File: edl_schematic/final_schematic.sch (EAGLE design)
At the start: 296 parts, among them IC1 FT232RL, IC14 TL084D, IC15 TL084D, IC16 TL084D, IC17 TL084D, IC18 TL084D, IC19 TL084D, IC20 TL084D, IC21 TL084D, IC22 TL084D, IC23 TL084D, IC24 TL084D, IC25 TL084D, IC26 TL084D, IC27 TL084D, IC28 TL084D, IC29 TL084D, IC3 TL084D, IC30 TL084D, IC4 TPS77333, IC5 TL084D, IC6 7812TV, Q1 BC558B, U1 TMS320F28069_PN_80, U3 TLV5610_DW_20, U4 MAX395EWG, U6 MAX395EWG, U7 MAX395EWG

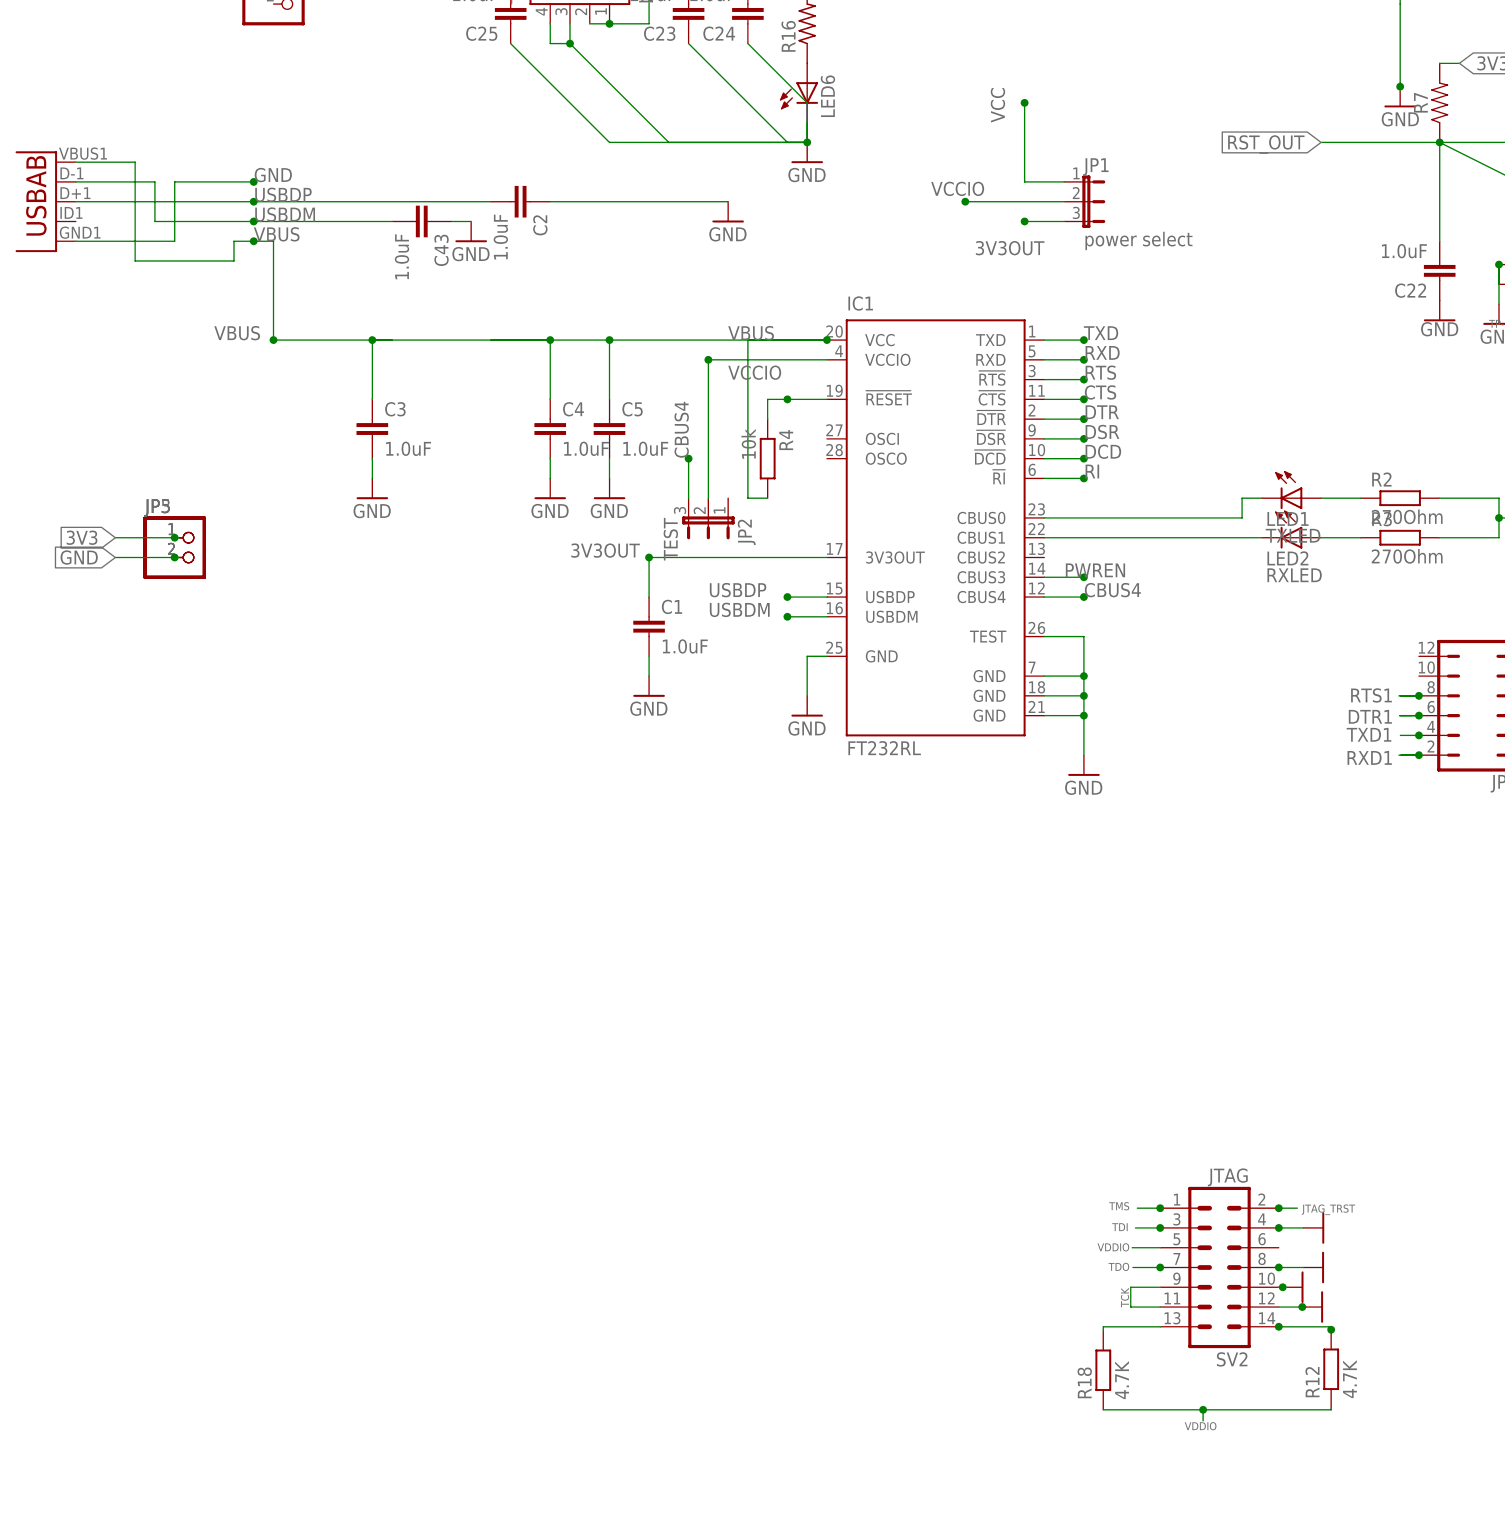
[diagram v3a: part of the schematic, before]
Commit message: usb_module added
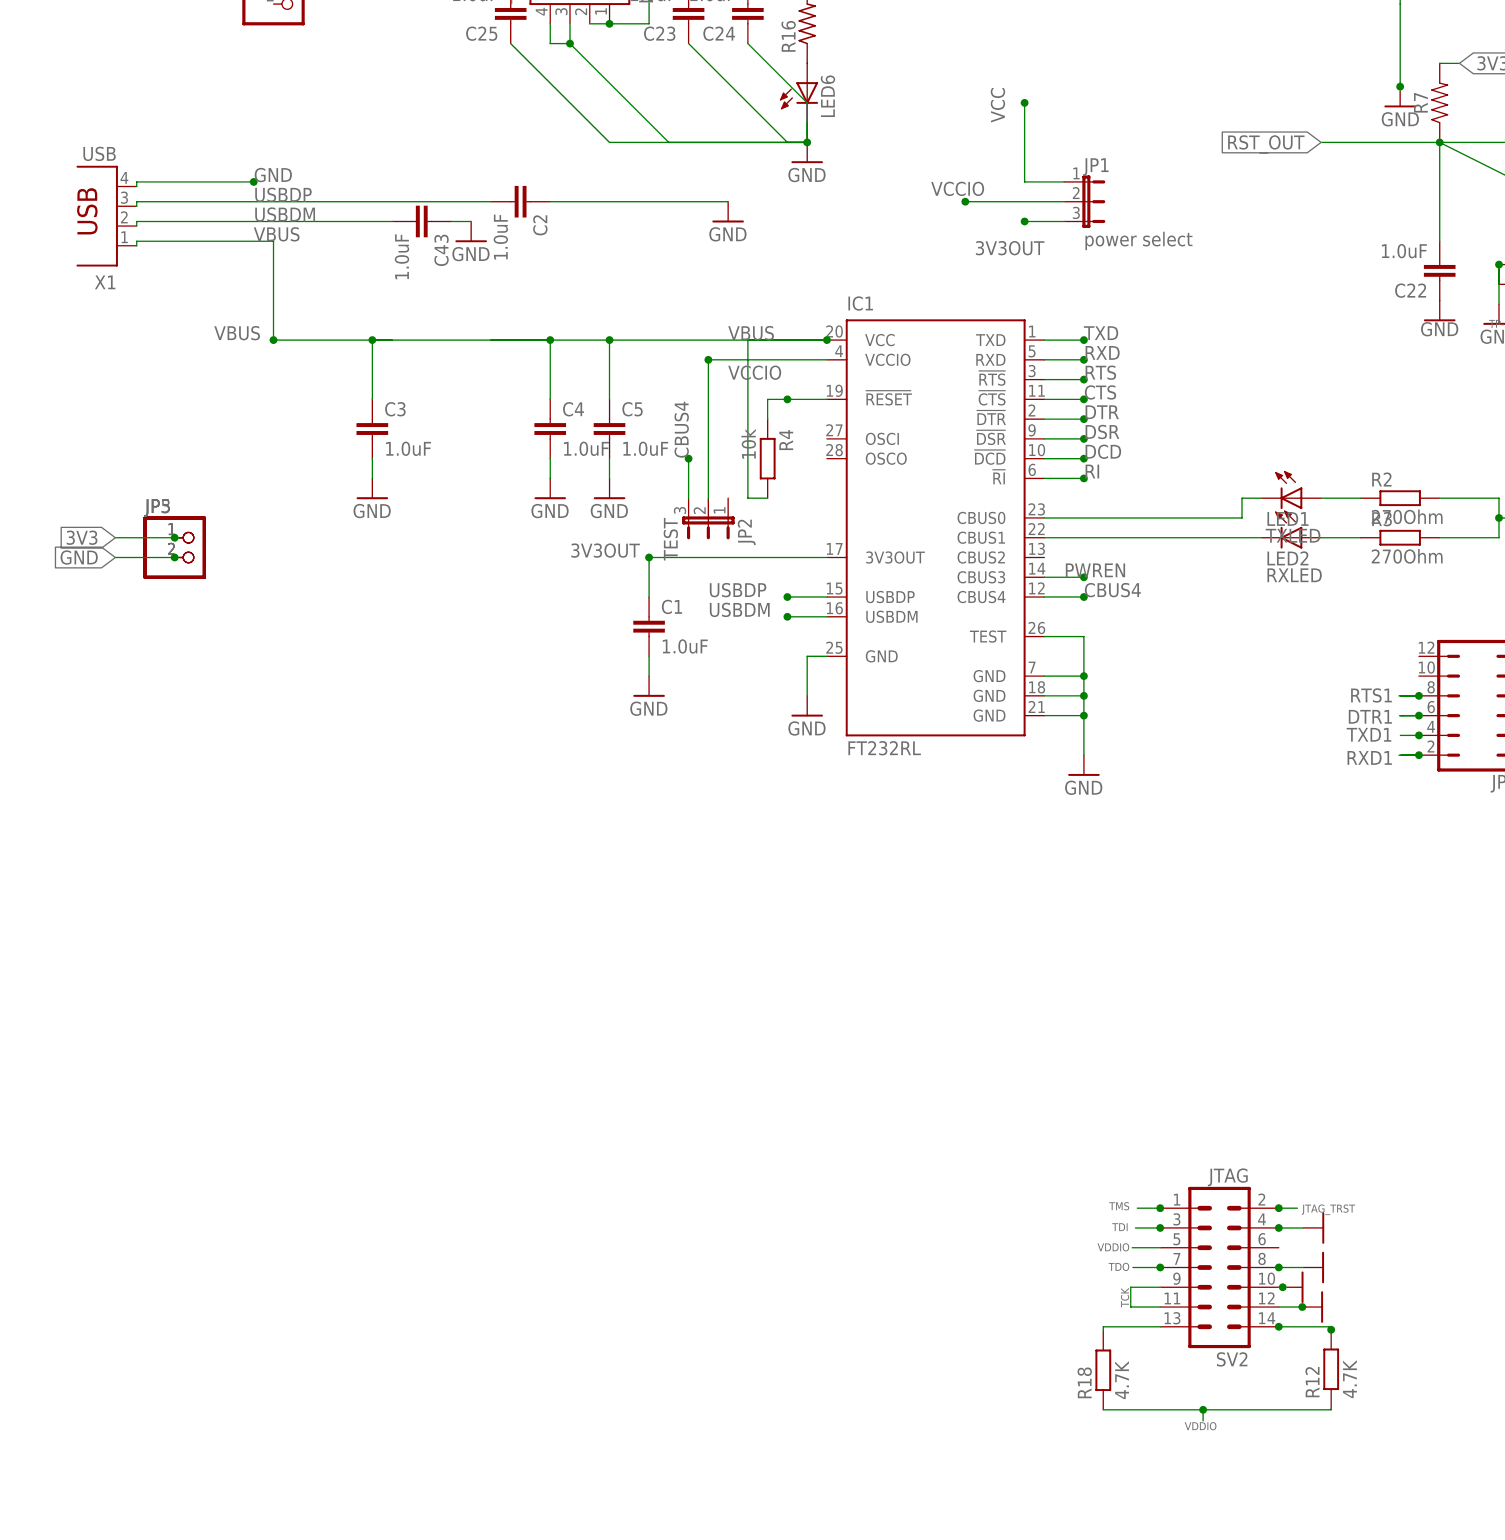
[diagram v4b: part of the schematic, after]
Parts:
- removed U2: (no value), MicroUSB:USB""
- added X1: USB, con-berg:PN61729
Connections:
- net GND: now also X1.4; no longer U2.GND
- net USBDM: now also X1.2; no longer U2.D-
- net USBDP: now also X1.3; no longer U2.D+
- net VBUS: now also X1.1; no longer U2.VBUS
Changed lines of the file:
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@@
 <?xml version="1.0" encoding="utf-8"?>
 <!DOCTYPE eagle SYSTEM "eagle.dtd">
-<eagle version="9.1.3">
+<eagle version="9.3.0">
 <drawing>
 <settings>
@@
 <part name="C30" library="SparkFun-Capacitors" deviceset="1.0UF" device="-1206-50V-10%" value="1.0uF"/>
 <part name="C31" library="SparkFun-Capacitors" deviceset="1.0UF" device="-1206-50V-10%" value="1.0uF"/>
-<part name="U2" library="MicroUSB" deviceset="USB" device="&quot;&quot;"/>
 <part name="U3" library="tlv5610a" deviceset="TLV5610_DW_20" device=""/>
 <part name="JP9" library="jumper" library_urn="urn:adsk.eagle:library:252" deviceset="JP7Q" device="" package3d_urn="urn:adsk.eagle:package:15458/1"/>
@@
 <part name="GND41" library="supply1" deviceset="GND" device=""/>
 <part name="GND42" library="supply1" deviceset="GND" device=""/>
+<part name="X1" library="con-berg" deviceset="PN61729" device="" value="USB"/>
 </parts>
 <sheets>
@@
 <attribute name="VALUE" x="63.119" y="169.164" size="1.778" layer="96" font="vector" rot="R90"/>
 </instance>
-<instance part="U2" gate="G$1" x="-7.62" y="88.9" smashed="yes" rot="R180"/>
 <instance part="U3" gate="A" x="370.84" y="172.72" smashed="yes">
 <attribute name="NAME" x="396.5956" y="181.8386" size="2.0828" layer="95" ratio="6" rot="SR0"/>
@@
 <attribute name="VALUE" x="439.42" y="-42.545" size="1.778" layer="96" rot="R180"/>
 </instance>
-<instance part="SV2" gate="G$1" x="144.4244" y="-48.0568" rot="R180"/>
-<instance part="R12" gate="G$1" x="158.7754" y="-61.1378" rot="R90"/>
-<instance part="R18" gate="G$1" x="129.4892" y="-61.2648" rot="R90"/>
+<instance part="SV2" gate="G$1" x="144.4244" y="-48.0568" smashed="yes" rot="R180">
+<attribute name="VALUE" x="148.2344" y="-35.3568" size="1.778" layer="96" rot="R180"/>
+<attribute name="NAME" x="148.2344" y="-58.9788" size="1.778" layer="95" rot="R180"/>
+</instance>
+<instance part="R12" gate="G$1" x="158.7754" y="-61.1378" smashed="yes" rot="R90">
+<attribute name="NAME" x="157.2768" y="-64.9478" size="1.778" layer="95" rot="R90"/>
+<attribute name="VALUE" x="162.0774" y="-64.9478" size="1.778" layer="96" rot="R90"/>
+</instance>
+<instance part="R18" gate="G$1" x="129.4892" y="-61.2648" smashed="yes" rot="R90">
+<attribute name="NAME" x="127.9906" y="-65.0748" size="1.778" layer="95" rot="R90"/>
+<attribute name="VALUE" x="132.7912" y="-65.0748" size="1.778" layer="96" rot="R90"/>
+</instance>
 <instance part="GND32" gate="1" x="157.7594" y="-42.9768" smashed="yes" rot="R90"/>
 <instance part="GND30" gate="1" x="157.734" y="-48.0568" smashed="yes" rot="R90"/>
 <instance part="GND41" gate="1" x="155.0924" y="-50.5968" smashed="yes" rot="R90"/>
 <instance part="GND42" gate="1" x="157.607" y="-53.1368" smashed="yes" rot="R90"/>
+<instance part="X1" gate="G$1" x="2.7432" y="88.3158" smashed="yes" rot="R180">
+<attribute name="NAME" x="2.7432" y="79.4258" size="1.778" layer="95" rot="R180"/>
+<attribute name="VALUE" x="2.7432" y="95.9358" size="1.778" layer="96" rot="R180"/>
+</instance>
 </instances>
 <busses>
@@
 <junction x="20.32" y="91.44"/>
 <label x="20.32" y="91.44" size="1.778" layer="95"/>
-<pinref part="U2" gate="G$1" pin="GND"/>
-<wire x1="-2.54" y1="83.82" x2="10.16" y2="83.82" width="0.1524" layer="91"/>
-<wire x1="10.16" y1="83.82" x2="10.16" y2="91.44" width="0.1524" layer="91"/>
-<wire x1="10.16" y1="91.44" x2="20.32" y2="91.44" width="0.1524" layer="91"/>
+<wire x1="5.2832" y1="91.44" x2="20.32" y2="91.44" width="0.1524" layer="91"/>
+<pinref part="X1" gate="G$1" pin="4"/>
+<wire x1="5.2832" y1="91.44" x2="5.2832" y2="90.8558" width="0.1524" layer="91"/>
 </segment>
 <segment>
@@
 <net name="VBUS" class="0">
 <segment>
-<wire x1="17.78" y1="83.82" x2="20.32" y2="83.82" width="0.1524" layer="91"/>
 <wire x1="38.1" y1="71.12" x2="35.56" y2="71.12" width="0.1524" layer="91"/>
 <wire x1="35.56" y1="71.12" x2="22.86" y2="71.12" width="0.1524" layer="91"/>
 <wire x1="35.56" y1="63.5" x2="35.56" y2="71.12" width="0.1524" layer="91"/>
-<wire x1="20.32" y1="83.82" x2="22.86" y2="83.82" width="0.1524" layer="91"/>
 <wire x1="22.86" y1="83.82" x2="22.86" y2="71.12" width="0.1524" layer="91"/>
-<junction x="20.32" y="83.82"/>
 <junction x="22.86" y="71.12"/>
 <junction x="35.56" y="71.12"/>
@@
 <wire x1="83.82" y1="71.12" x2="93.98" y2="71.12" width="0.1524" layer="91"/>
 <junction x="93.98" y="71.12"/>
-<pinref part="U2" gate="G$1" pin="VBUS"/>
-<wire x1="-2.54" y1="93.98" x2="5.08" y2="93.98" width="0.1524" layer="91"/>
-<wire x1="5.08" y1="93.98" x2="5.08" y2="81.28" width="0.1524" layer="91"/>
-<wire x1="5.08" y1="81.28" x2="17.78" y2="81.28" width="0.1524" layer="91"/>
-<wire x1="17.78" y1="81.28" x2="17.78" y2="83.82" width="0.1524" layer="91"/>
 <pinref part="C3" gate="G$1" pin="1"/>
 <pinref part="C4" gate="G$1" pin="1"/>
 <pinref part="C5" gate="G$1" pin="1"/>
+<pinref part="X1" gate="G$1" pin="1"/>
+<wire x1="22.86" y1="83.82" x2="5.2832" y2="83.82" width="0.1524" layer="91"/>
+<wire x1="5.2832" y1="83.82" x2="5.2832" y2="83.2358" width="0.1524" layer="91"/>
 </segment>
 <segment>
@@
 <net name="USBDM" class="0">
 <segment>
-<wire x1="20.32" y1="86.36" x2="38.1" y2="86.36" width="0.1524" layer="91"/>
-<junction x="20.32" y="86.36"/>
+<wire x1="5.2832" y1="86.36" x2="38.1" y2="86.36" width="0.1524" layer="91"/>
 <label x="20.32" y="86.36" size="1.778" layer="95"/>
-<pinref part="U2" gate="G$1" pin="D-"/>
-<wire x1="-2.54" y1="91.44" x2="7.62" y2="91.44" width="0.1524" layer="91"/>
-<wire x1="7.62" y1="91.44" x2="7.62" y2="86.36" width="0.1524" layer="91"/>
-<wire x1="7.62" y1="86.36" x2="20.32" y2="86.36" width="0.1524" layer="91"/>
 <pinref part="C43" gate="G$1" pin="2"/>
+<pinref part="X1" gate="G$1" pin="2"/>
+<wire x1="5.2832" y1="86.36" x2="5.2832" y2="85.7758" width="0.1524" layer="91"/>
 </segment>
 <segment>
@@
 <net name="USBDP" class="0">
 <segment>
-<wire x1="20.32" y1="88.9" x2="50.8" y2="88.9" width="0.1524" layer="91"/>
-<junction x="20.32" y="88.9"/>
+<wire x1="5.2832" y1="88.9" x2="50.8" y2="88.9" width="0.1524" layer="91"/>
 <label x="20.32" y="88.9" size="1.778" layer="95"/>
-<pinref part="U2" gate="G$1" pin="D+"/>
-<wire x1="-2.54" y1="88.9" x2="20.32" y2="88.9" width="0.1524" layer="91"/>
 <pinref part="C2" gate="G$1" pin="2"/>
-</segment>
-<segment>
+<pinref part="X1" gate="G$1" pin="3"/>
+<wire x1="5.2832" y1="88.9" x2="5.2832" y2="88.3158" width="0.1524" layer="91"/>
+</segment>
+<segment>

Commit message: USB_UPDATED
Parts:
- removed X1: USB, con-berg:PN61729
- added CON1: UBC05V128-B0C04D, con-cypressindustries:MINI-USB-32005-201
- added F1: 500mA, rcl:L-EUL1812
- added R19: 0, rcl:R-US_R1206
- added R20: 0, rcl:R-US_R1206W
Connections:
- new net N$12: CON1.2, R19.1
- new net N$13: CON1.3, R20.1
- new net XUSB: CON1.1, F1.2
- net GND: now also CON1.5; no longer X1.4
- net USBDM: now also R19.2; no longer X1.2
- net USBDP: now also R20.2; no longer X1.3
- net VBUS: now also F1.1; no longer X1.1
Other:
- note added: "Mini USB"
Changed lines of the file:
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@@
 <setting verticaltext="up"/>
 </settings>
-<grid distance="0.1" unitdist="inch" unit="inch" style="lines" multiple="1" display="no" altdistance="0.01" altunitdist="inch" altunit="inch"/>
+<grid distance="0.1" unitdist="inch" unit="mil" style="lines" multiple="1" display="no" altdistance="0.01" altunitdist="inch" altunit="mil"/>
 <layers>
 <layer number="1" name="Top" color="4" fill="1" visible="no" active="no"/>
@@
 <part name="GND41" library="supply1" deviceset="GND" device=""/>
 <part name="GND42" library="supply1" deviceset="GND" device=""/>
-<part name="X1" library="con-berg" deviceset="PN61729" device="" value="USB"/>
+<part name="CON1" library="con-cypressindustries" deviceset="MINI-USB-" device="32005-201" value="UBC05V128-B0C04D"/>
+<part name="F1" library="rcl" deviceset="L-EU" device="L1812" value="500mA"/>
+<part name="R19" library="rcl" deviceset="R-US_" device="R1206" value="0"/>
+<part name="R20" library="rcl" deviceset="R-US_" device="R1206W" value="0"/>
 </parts>
 <sheets>
 <sheet>
 <plain>
+<text x="-56.9214" y="97.1804" size="1.016" layer="104">Mini USB</text>
 </plain>
 <instances>
@@
 <instance part="GND41" gate="1" x="155.0924" y="-50.5968" smashed="yes" rot="R90"/>
 <instance part="GND42" gate="1" x="157.607" y="-53.1368" smashed="yes" rot="R90"/>
-<instance part="X1" gate="G$1" x="2.7432" y="88.3158" smashed="yes" rot="R180">
-<attribute name="NAME" x="2.7432" y="79.4258" size="1.778" layer="95" rot="R180"/>
-<attribute name="VALUE" x="2.7432" y="95.9358" size="1.778" layer="96" rot="R180"/>
+<instance part="CON1" gate="G$1" x="-48.0314" y="85.7504" smashed="yes" rot="MR0">
+<attribute name="NAME" x="-54.3814" y="75.5904" size="1.016" layer="95" font="vector" rot="MR180"/>
+<attribute name="VALUE" x="-60.7314" y="73.0504" size="1.016" layer="96" font="vector" rot="MR180"/>
+</instance>
+<instance part="F1" gate="G$1" x="-27.7114" y="98.4504" smashed="yes" rot="R270">
+<attribute name="NAME" x="-31.5214" y="99.949" size="1.778" layer="95"/>
+<attribute name="VALUE" x="-31.5214" y="95.1484" size="1.778" layer="96"/>
+</instance>
+<instance part="R19" gate="G$1" x="-22.6314" y="88.2904" smashed="yes">
+<attribute name="NAME" x="-30.5054" y="89.027" size="1.016" layer="95"/>
+<attribute name="VALUE" x="-19.5834" y="89.0524" size="1.016" layer="96"/>
+</instance>
+<instance part="R20" gate="G$1" x="-22.6314" y="85.7504" smashed="yes">
+<attribute name="NAME" x="-30.5054" y="86.487" size="1.016" layer="95"/>
+<attribute name="VALUE" x="-19.5834" y="86.5124" size="1.016" layer="96"/>
 </instance>
 </instances>
@@
 <label x="20.32" y="91.44" size="1.778" layer="95"/>
 <wire x1="5.2832" y1="91.44" x2="20.32" y2="91.44" width="0.1524" layer="91"/>
-<pinref part="X1" gate="G$1" pin="4"/>
 <wire x1="5.2832" y1="91.44" x2="5.2832" y2="90.8558" width="0.1524" layer="91"/>
 </segment>
@@
 <junction x="155.067" y="-53.1368"/>
 </segment>
+<segment>
+<wire x1="-42.9514" y1="80.6704" x2="-34.0614" y2="80.6704" width="0.1524" layer="91"/>
+<wire x1="-34.0614" y1="80.6704" x2="-34.0614" y2="70.5104" width="0.1524" layer="91"/>
+<pinref part="CON1" gate="G$1" pin="5"/>
+<label x="-33.02" y="71.12" size="1.778" layer="95" xref="yes"/>
+</segment>
 </net>
 <net name="VCC" class="1">
@@
 <pinref part="C4" gate="G$1" pin="1"/>
 <pinref part="C5" gate="G$1" pin="1"/>
-<pinref part="X1" gate="G$1" pin="1"/>
 <wire x1="22.86" y1="83.82" x2="5.2832" y2="83.82" width="0.1524" layer="91"/>
 <wire x1="5.2832" y1="83.82" x2="5.2832" y2="83.2358" width="0.1524" layer="91"/>
@@
 <label x="33.02" y="124.46" size="1.778" layer="95" xref="yes"/>
 </segment>
+<segment>
+<wire x1="-12.3952" y1="98.425" x2="-22.6314" y2="98.4504" width="0.1524" layer="91"/>
+<pinref part="F1" gate="G$1" pin="1"/>
+<label x="-20.574" y="98.8822" size="1.016" layer="95"/>
+<junction x="-12.3952" y="98.425"/>
+</segment>
 </net>
 <net name="USBDM" class="0">
@@
 <label x="20.32" y="86.36" size="1.778" layer="95"/>
 <pinref part="C43" gate="G$1" pin="2"/>
-<pinref part="X1" gate="G$1" pin="2"/>
 <wire x1="5.2832" y1="86.36" x2="5.2832" y2="85.7758" width="0.1524" layer="91"/>
 </segment>
@@
 <pinref part="IC1" gate="1" pin="USBDM"/>
 </segment>
+<segment>
+<pinref part="R19" gate="G$1" pin="2"/>
+<wire x1="-17.5514" y1="88.2904" x2="-15.0114" y2="88.2904" width="0.1524" layer="91"/>
+<label x="-15.0114" y="88.2904" size="1.016" layer="95"/>
+</segment>
 </net>
 <net name="USBDP" class="0">
@@
 <label x="20.32" y="88.9" size="1.778" layer="95"/>
 <pinref part="C2" gate="G$1" pin="2"/>
-<pinref part="X1" gate="G$1" pin="3"/>
 <wire x1="5.2832" y1="88.9" x2="5.2832" y2="88.3158" width="0.1524" layer="91"/>
 </segment>
@@
 <pinref part="IC1" gate="1" pin="USBDP"/>
 </segment>
+<segment>
+<pinref part="R20" gate="G$1" pin="2"/>
+<wire x1="-17.5514" y1="85.7504" x2="-15.0114" y2="85.7504" width="0.1524" layer="91"/>
+<label x="-15.0114" y="85.7504" size="1.016" layer="95"/>
+</segment>
 </net>
 <net name="3V3OUT" class="0">
@@
 </segment>
 </net>
+<net name="XUSB" class="0">
+<segment>
+<wire x1="-42.9514" y1="90.8304" x2="-37.8714" y2="90.8304" width="0.1524" layer="91"/>
+<wire x1="-37.8714" y1="90.8304" x2="-37.8714" y2="98.4504" width="0.1524" layer="91"/>
+<wire x1="-37.8714" y1="98.4504" x2="-32.7914" y2="98.4504" width="0.1524" layer="91"/>
+<pinref part="CON1" gate="G$1" pin="1"/>
+<pinref part="F1" gate="G$1" pin="2"/>
+</segment>
+</net>
+<net name="N$12" class="0">
+<segment>
+<pinref part="CON1" gate="G$1" pin="2"/>
+<wire x1="-42.9514" y1="88.2904" x2="-27.7114" y2="88.2904" width="0.1524" layer="91"/>
+<pinref part="R19" gate="G$1" pin="1"/>
+</segment>
+</net>
+<net name="N$13" class="0">
+<segment>
+<pinref part="CON1" gate="G$1" pin="3"/>
+<pinref part="R20" gate="G$1" pin="1"/>
+<wire x1="-27.7114" y1="85.7504" x2="-42.9514" y2="85.7504" width="0.1524" layer="91"/>
+</segment>
+</net>
